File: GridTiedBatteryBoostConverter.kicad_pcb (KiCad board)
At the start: 2 copper layers, 270.1 x 143.1 mm, 161 parts, among them J101 Battery Connection, J103 Solar Panels, J202 Conn_01x03_Female, J203 I2C_BUS, J401 Screw_Terminal_01x02, J402 AudioJack2_SwitchT, Q101 IXFP36N20X3, Q102 BC847B-13-F, Q103 SSM3K329R, Q104 SSM3J334R, Q201 SSM3K329R, Q202 SSM3K329R, Q203 SSM3J334R, Q301 BC847B-13-F, Q302 BC856B-13-F, Q305 TK32A12N1,S4X, Q306 TK32A12N1,S4X, SW201 SW_Up, SW202 SW_Down, SW203 SW_Enter, U101 OPA2837IDGKR, U102 UCC2800DTR, U201 LCD 2004A Right Angle Header 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, U202 Teensy-LC, U203 PCF8574ADWR, U204 ESP-WROOM-02U, U301 FDA217, U302 LTC7138EMSE-PBF, U303 TPS560200DBVR, U304 TLV70430DBVT, U305 REF2925AIDBZT, U306 TPS560200DBVR

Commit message: change how the current sense traces attach to the average output current sense resistor R120, they are now at right angles to the current sense resistor and attach directly to it.
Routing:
- net Net-(J103-Pad2): track 102.8 -> 135.4 mm, vias 2 -> 3
- net 0: track 311.2 -> 342.9 mm, vias 87 -> 88
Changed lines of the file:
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@@
     (thickness 1.6)
     (drawings 38)
-    (tracks 1093)
+    (tracks 1105)
     (zones 0)
     (modules 161)
@@
   )
   (setup
-    (last_trace_width 5)
+    (last_trace_width 1)
     (user_trace_width 0.5)
     (user_trace_width 1)
@@
   (segment (start 275.5 64.6) (end 256.1 64.6) (width 5) (layer F.Cu) (net 3))
   (segment (start 256.1 64.6) (end 255.95 64.45) (width 5) (layer F.Cu) (net 3))
-  (via (at 234.7 64.6) (size 0.8) (drill 0.4) (layers F.Cu B.Cu) (net 3))
-  (segment (start 255.2 64.6) (end 234.7 64.6) (width 1) (layer B.Cu) (net 3))
-  (segment (start 234.7 64.6) (end 222.1 64.6) (width 1) (layer F.Cu) (net 3))
-  (segment (start 222.1 64.6) (end 211.75 74.95) (width 1) (layer F.Cu) (net 3))
-  (segment (start 211.75 74.95) (end 211.75 78) (width 1) (layer F.Cu) (net 3))
-  (segment (start 211.75 78) (end 206.35 83.4) (width 1) (layer F.Cu) (net 3))
-  (segment (start 206.35 83.4) (end 201.75 83.4) (width 1) (layer F.Cu) (net 3))
   (segment (start 194.4 115.65) (end 196.8 115.7) (width 1) (layer F.Cu) (net 3))
   (via (at 196.8 115.7) (size 0.8) (drill 0.4) (layers F.Cu B.Cu) (net 3))
@@
   (segment (start 185.3 71.90002) (end 180.1 66.70002) (width 1) (layer F.Cu) (net 3))
   (segment (start 185.3 78.05) (end 185.3 71.90002) (width 1) (layer F.Cu) (net 3))
+  (segment (start 278.4 64.6) (end 278.4 61.6) (width 1) (layer F.Cu) (net 3))
+  (via (at 251.7 60.45) (size 0.8) (drill 0.4) (layers F.Cu B.Cu) (net 3))
+  (segment (start 278.4 61.6) (end 277.25 60.45) (width 1) (layer F.Cu) (net 3))
+  (segment (start 277.25 60.45) (end 251.7 60.45) (width 1) (layer F.Cu) (net 3))
+  (via (at 234.65 61.6) (size 0.8) (drill 0.4) (layers F.Cu B.Cu) (net 3))
+  (segment (start 251.7 60.45) (end 235.8 60.45) (width 1) (layer B.Cu) (net 3))
+  (segment (start 235.8 60.45) (end 234.65 61.6) (width 1) (layer B.Cu) (net 3))
+  (segment (start 206.35 83.4) (end 201.75 83.4) (width 1) (layer F.Cu) (net 3))
+  (segment (start 211.75 78) (end 206.35 83.4) (width 1) (layer F.Cu) (net 3))
+  (segment (start 234.65 61.6) (end 219.5 61.6) (width 1) (layer F.Cu) (net 3))
+  (segment (start 211.75 69.35) (end 211.75 78) (width 1) (layer F.Cu) (net 3))
+  (segment (start 219.5 61.6) (end 211.75 69.35) (width 1) (layer F.Cu) (net 3))
   (segment (start 231.1 32) (end 216.9 32) (width 12) (layer F.Cu) (net 4))
   (segment (start 231.1 32) (end 242.9 32) (width 12) (layer F.Cu) (net 4))
@@
   (segment (start 258.6 84.85) (end 259.15 85.4) (width 1) (layer B.Cu) (net 125))
   (segment (start 203.4 84.85) (end 200.95 87.3) (width 1) (layer F.Cu) (net 125))
-  (via (at 224.85 84.9) (size 0.8) (drill 0.4) (layers F.Cu B.Cu) (net 125))
-  (segment (start 224.85 84.9) (end 258.6 84.85) (width 1) (layer B.Cu) (net 125))
   (segment (start 200.95 87.3) (end 196.55 87.3) (width 1) (layer F.Cu) (net 125))
-  (segment (start 224.85 84.9) (end 203.4 84.85) (width 1) (layer F.Cu) (net 125))
+  (via (at 249.1 70.35) (size 0.8) (drill 0.4) (layers F.Cu B.Cu) (net 125))
+  (segment (start 279.1 70.35) (end 249.1 70.35) (width 1) (layer F.Cu) (net 125))
+  (via (at 235.5 69) (size 0.8) (drill 0.4) (layers F.Cu B.Cu) (net 125))
+  (segment (start 249.1 70.35) (end 247.75 69) (width 1) (layer B.Cu) (net 125))
+  (segment (start 247.75 69) (end 235.5 69) (width 1) (layer B.Cu) (net 125))
+  (segment (start 235.5 69) (end 214.5 69) (width 1) (layer F.Cu) (net 125))
+  (segment (start 214.5 69) (end 213.65 69.85) (width 1) (layer F.Cu) (net 125))
+  (segment (start 213.65 78.4) (end 207.191163 84.858837) (width 1) (layer F.Cu) (net 125))
+  (segment (start 213.65 69.85) (end 213.65 78.4) (width 1) (layer F.Cu) (net 125))
+  (segment (start 207.191163 84.858837) (end 203.4 84.85) (width 1) (layer F.Cu) (net 125))
   (zone (net 0) (net_name "") (layer B.Cu) (hatch edge 0.508)
     (connect_pads (clearance 0.508))

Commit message: further improved routing of sense trace to current sense resistor R120
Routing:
- net 0: track 342.9 -> 338.7 mm
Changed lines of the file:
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@@
   (segment (start 185.3 71.90002) (end 180.1 66.70002) (width 1) (layer F.Cu) (net 3))
   (segment (start 185.3 78.05) (end 185.3 71.90002) (width 1) (layer F.Cu) (net 3))
-  (segment (start 278.4 64.6) (end 278.4 61.6) (width 1) (layer F.Cu) (net 3))
-  (via (at 251.7 60.45) (size 0.8) (drill 0.4) (layers F.Cu B.Cu) (net 3))
-  (segment (start 278.4 61.6) (end 277.25 60.45) (width 1) (layer F.Cu) (net 3))
-  (segment (start 277.25 60.45) (end 251.7 60.45) (width 1) (layer F.Cu) (net 3))
-  (via (at 234.65 61.6) (size 0.8) (drill 0.4) (layers F.Cu B.Cu) (net 3))
-  (segment (start 251.7 60.45) (end 235.8 60.45) (width 1) (layer B.Cu) (net 3))
-  (segment (start 235.8 60.45) (end 234.65 61.6) (width 1) (layer B.Cu) (net 3))
+  (segment (start 279.1 66.35) (end 277.8 66.35) (width 1) (layer F.Cu) (net 3))
+  (via (at 249.75 68.4) (size 0.8) (drill 0.4) (layers F.Cu B.Cu) (net 3))
+  (segment (start 277.8 66.35) (end 275.75 68.4) (width 1) (layer F.Cu) (net 3))
+  (segment (start 275.75 68.4) (end 249.75 68.4) (width 1) (layer F.Cu) (net 3))
+  (segment (start 249.75 68.4) (end 248.4 67.05) (width 1) (layer B.Cu) (net 3))
+  (via (at 235.65 67.05) (size 0.8) (drill 0.4) (layers F.Cu B.Cu) (net 3))
+  (segment (start 248.4 67.05) (end 235.65 67.05) (width 1) (layer B.Cu) (net 3))
+  (segment (start 235.65 67.05) (end 214.4 67.05) (width 1) (layer F.Cu) (net 3))
   (segment (start 206.35 83.4) (end 201.75 83.4) (width 1) (layer F.Cu) (net 3))
   (segment (start 211.75 78) (end 206.35 83.4) (width 1) (layer F.Cu) (net 3))
-  (segment (start 234.65 61.6) (end 219.5 61.6) (width 1) (layer F.Cu) (net 3))
+  (segment (start 214.4 67.05) (end 211.75 69.35) (width 1) (layer F.Cu) (net 3))
   (segment (start 211.75 69.35) (end 211.75 78) (width 1) (layer F.Cu) (net 3))
-  (segment (start 219.5 61.6) (end 211.75 69.35) (width 1) (layer F.Cu) (net 3))
   (segment (start 231.1 32) (end 216.9 32) (width 12) (layer F.Cu) (net 4))
   (segment (start 231.1 32) (end 242.9 32) (width 12) (layer F.Cu) (net 4))

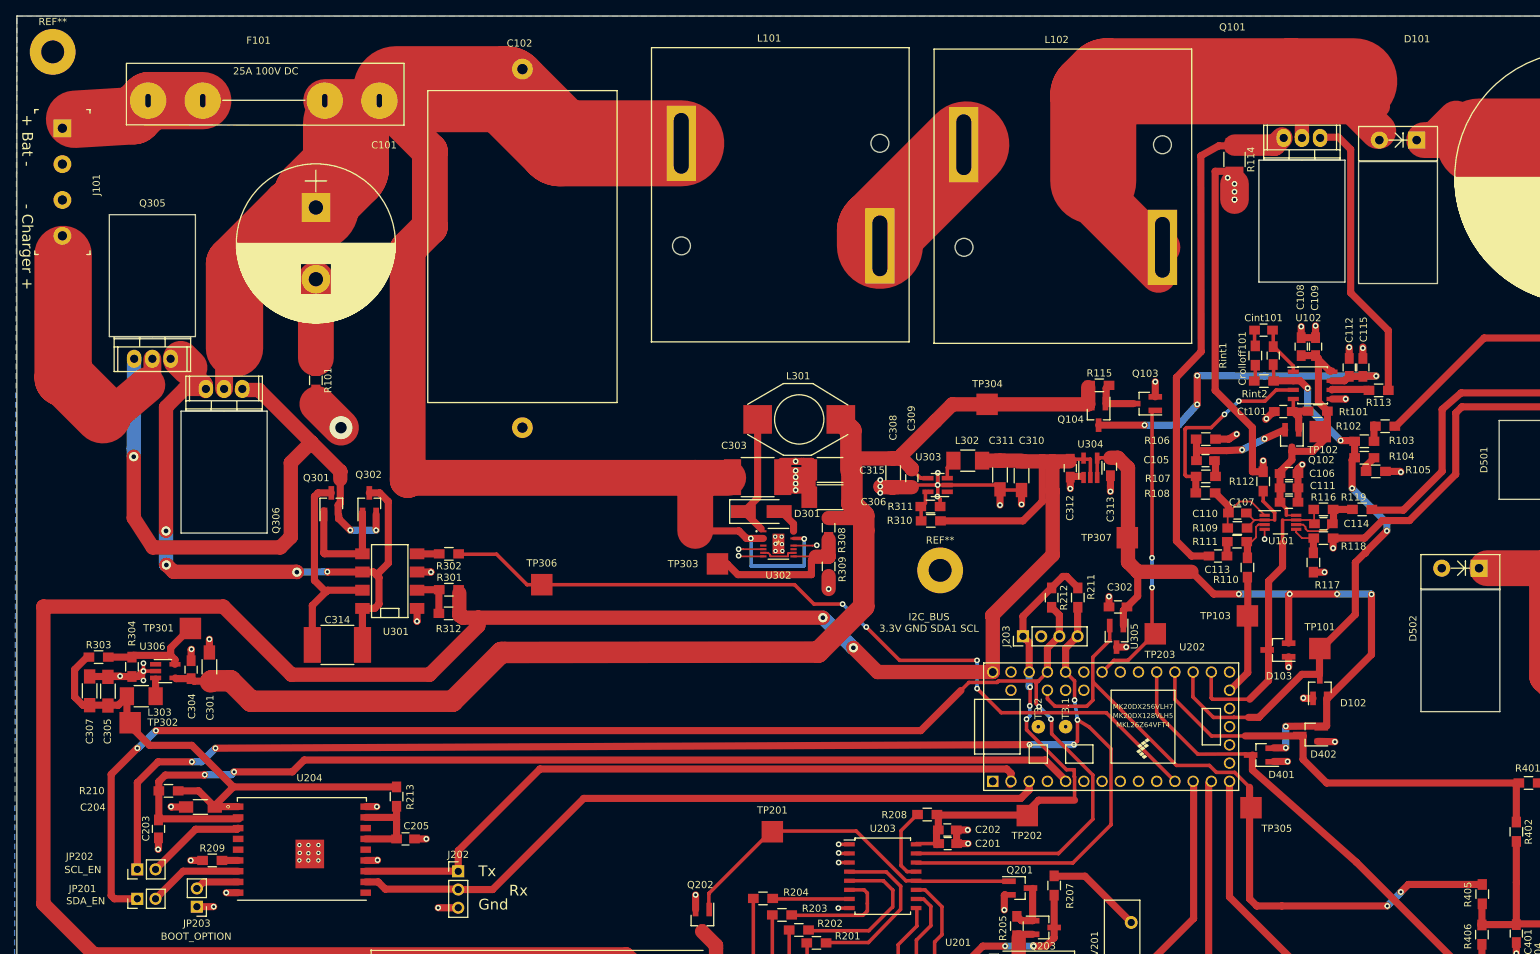
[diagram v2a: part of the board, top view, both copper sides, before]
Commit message: Replaced TK32A12N1,S4X TO-220 Toshiba transistors that were use for turning the charger on and off, with a pair of IRFP4321PBF's from Infinion, in a TO-247AC package.  The reson for the change was this part of the circuit carries ~20A at 102.2V peak, so for a 30 degree rise in trace temp with 2 Once copper we need 5mm trace width, but we also need 1.1mm clearance, and this was differcult to acheive with the to-220 package, with out bending the legs etc. These devices are 2 time the price at about  with 15.5 mOhm vs 11 mOhm rds on.  Increased the main FETs gate drive trace to 2mm from 1mm.
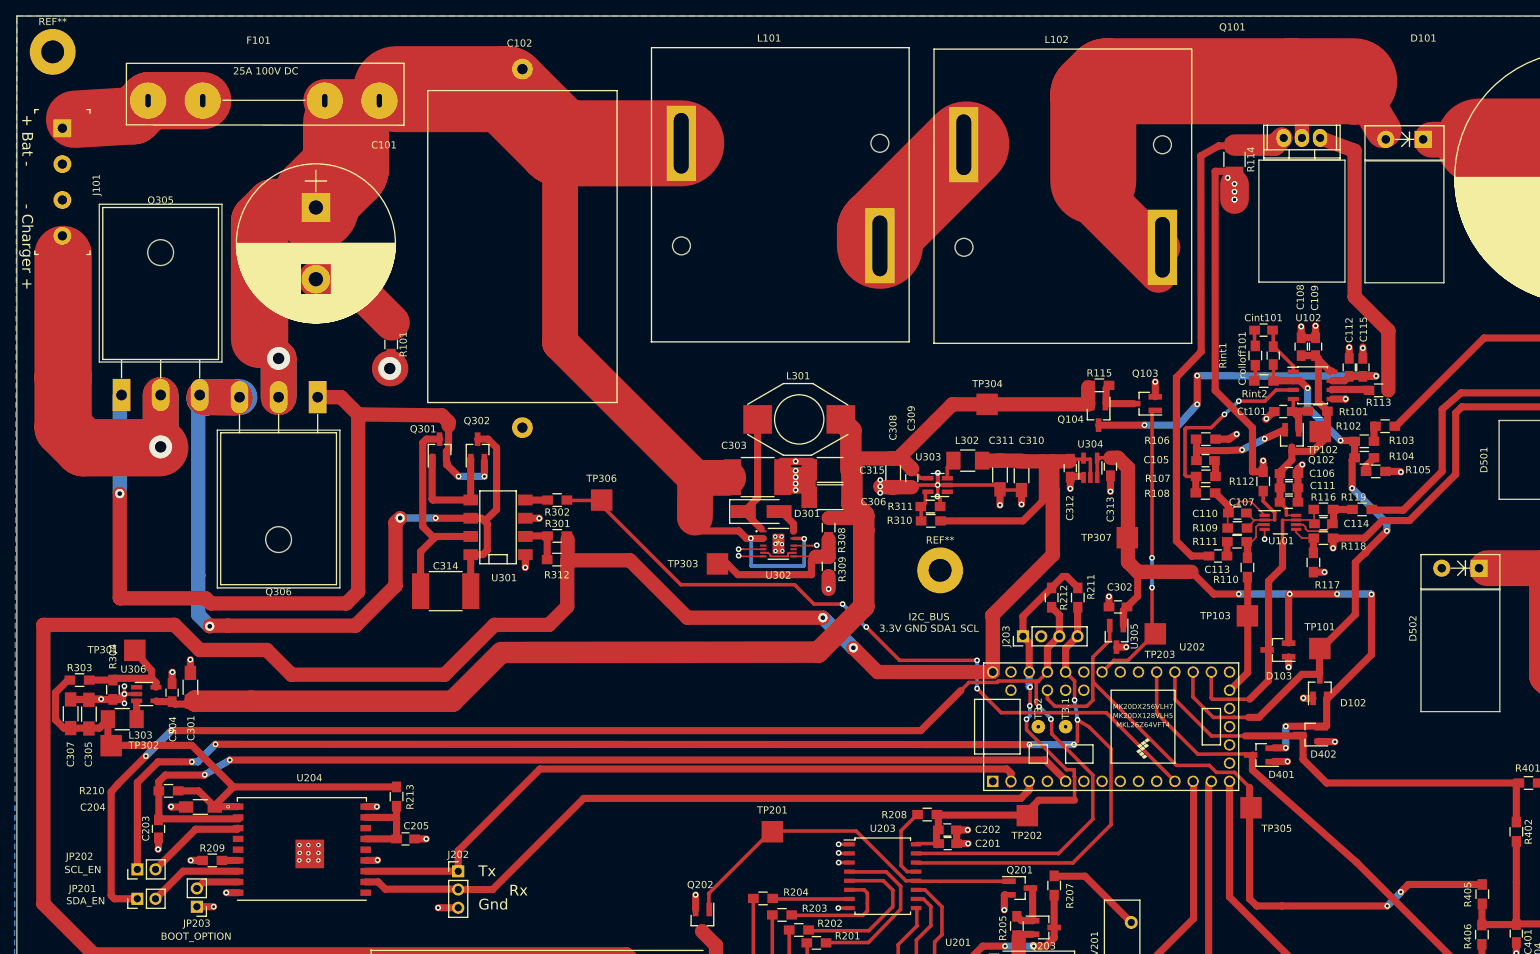
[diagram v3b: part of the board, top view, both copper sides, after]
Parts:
- Q305, Q306: value TK32A12N1,S4X -> IRFP4321PBF; footprint Transistors_ThroughHole_jl:TO-220 -> Transistors_ThroughHole_jl:TO-247-3_Horizontal_TabDown
- moved Q301 16.9 mm to (72.0, 75.0)
- moved Q302 16.9 mm to (77.2, 75.0)
- moved C314 16.9 mm to (72.8, 94.7)
- moved R301 16.9 mm to (88.3, 87.0)
- moved R302 16.9 mm to (88.3, 82.0)
- moved R312 16.9 mm to (88.3, 90.3)
- moved U301 16.9 mm to (80.1, 85.8)
- moved TP306 14.5 mm to (94.5, 82.0)
- moved Q306 13.1 mm to (55.0, 67.7)
- moved R101 11.6 mm to (65.2, 60.3)
- moved TP301 8.33 mm to (29.4, 103.0)
- moved Q305 6.63 mm to (27.6, 67.3)
- moved L303 4.15 mm to (27.7, 112.5)
- moved R304 4.15 mm to (26.4, 108.5)
- moved TP302 4.15 mm to (26.1, 116.2)
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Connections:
- net Net-(C314-Pad2) renamed /PowerSupplies/Charger_FETs_Source
- net Net-(Q101-Pad1) renamed /GateDrive
- net Net-(Q301-Pad2) renamed /PowerSupplies/Charger_Fets_GateDrive
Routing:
- net Vin: track 244.7 -> 210.5 mm, vias 2 -> 3
- net /PowerSupplies/Charger_FETs_Source: track 90.5 -> 123.9 mm, vias 4 -> 3
- net /PowerSupplies/Charger_Fets_GateDrive: track 97.3 -> 120.8 mm
- net ChargerConnection: track 36.5 -> 53.4 mm, vias 0 -> 1
- net /PowerSupplies/CHARGER_ON_OFF: track 115.4 -> 104.2 mm
- net 0: track 338.7 -> 334.1 mm
- net +5V: track 414.9 -> 418.3 mm
- net Net-(C101-Pad2): track 11.0 -> 13.1 mm
- net Net-(D101-Pad2): track 109.0 -> 107.3 mm
- net SDA1: track 216.7 -> 215.3 mm
- net Vboost_out: track 169.5 -> 170.6 mm
- net +3.3V_wifi_only: track 73.4 -> 74.3 mm
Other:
- net class ChargerConnection added: clearance 1.1, trace_width 8, via_dia 5, via_drill 2.5
- net class ChargerFetsGateDrive added: clearance 1.1, trace_width 1, via_dia 1.2, via_drill 0.6
- net class u302 removed

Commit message: Change footprint for the main switching FET to have a bent drain to achieve trace width and clearance requirements.  Fixed a pin numbering miss alignment between schematic and footprint for the isolating transformer. Spoted trace clearance issue on the 230V AC mains input into the isolating transformer for the house voltage sense, increased to 2.5mm.
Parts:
- Q101: footprint Transistors_ThroughHole_jl:TO-220 -> Transistors_ThroughHole_jl:TO-220_Horizontal_Offset_Drain
- moved R402 7.70 mm to (222.3, 120.5)
- moved R401 5.23 mm to (228.5, 119.2)
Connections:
- net Net-(J401-Pad1) renamed /MainsPowerMonitor/AC_Mains_Phase
- net Net-(J401-Pad2) renamed /MainsPowerMonitor/AC_Mains_Neutral
- TR401 pad 5: Net-(C401-Pad1) -> Net-(R401-Pad1)
- TR401 pad 6: Net-(R401-Pad1) -> Net-(C401-Pad1)
- TR401 pad 7: Net-(C401-Pad1) -> Net-(R401-Pad1)
- TR401 pad 8: Net-(R401-Pad1) -> Net-(C401-Pad1)
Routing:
- net /MainsPowerMonitor/AC_Mains_Phase: track 24.3 -> 57.8 mm
- net Vboost_out: track 170.6 -> 150.2 mm
- net Net-(R401-Pad1): track 21.0 -> 38.8 mm
- net Mains_Current: track 128.8 -> 141.1 mm
- net Net-(D101-Pad2): track 107.3 -> 101.4 mm
- net Net-(C401-Pad1): track 114.4 -> 119.4 mm
- net +5V: track 418.3 -> 420.4 mm
- net Mains_Voltage: track 63.9 -> 62.3 mm
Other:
- net class AC_Mains added: clearance 2.5, trace_width 1, via_dia 1.2, via_drill 0.6
- board text added: "Voltage Sense Phase Neutral"

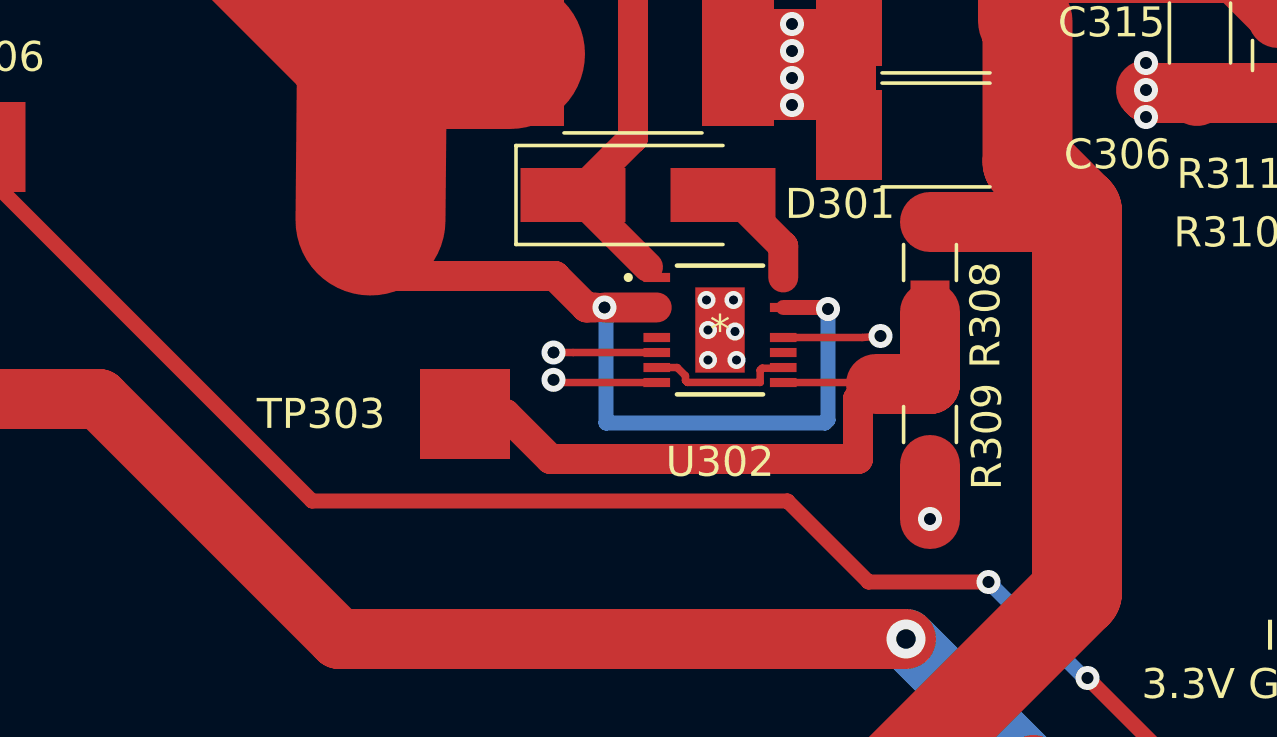
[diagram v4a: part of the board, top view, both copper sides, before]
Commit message: Improved clearance of Vin into U302 as good as the package will allow. Also reduced clearance around the Teesy to 0.5mm, because I notice one for the grounds was not connected.
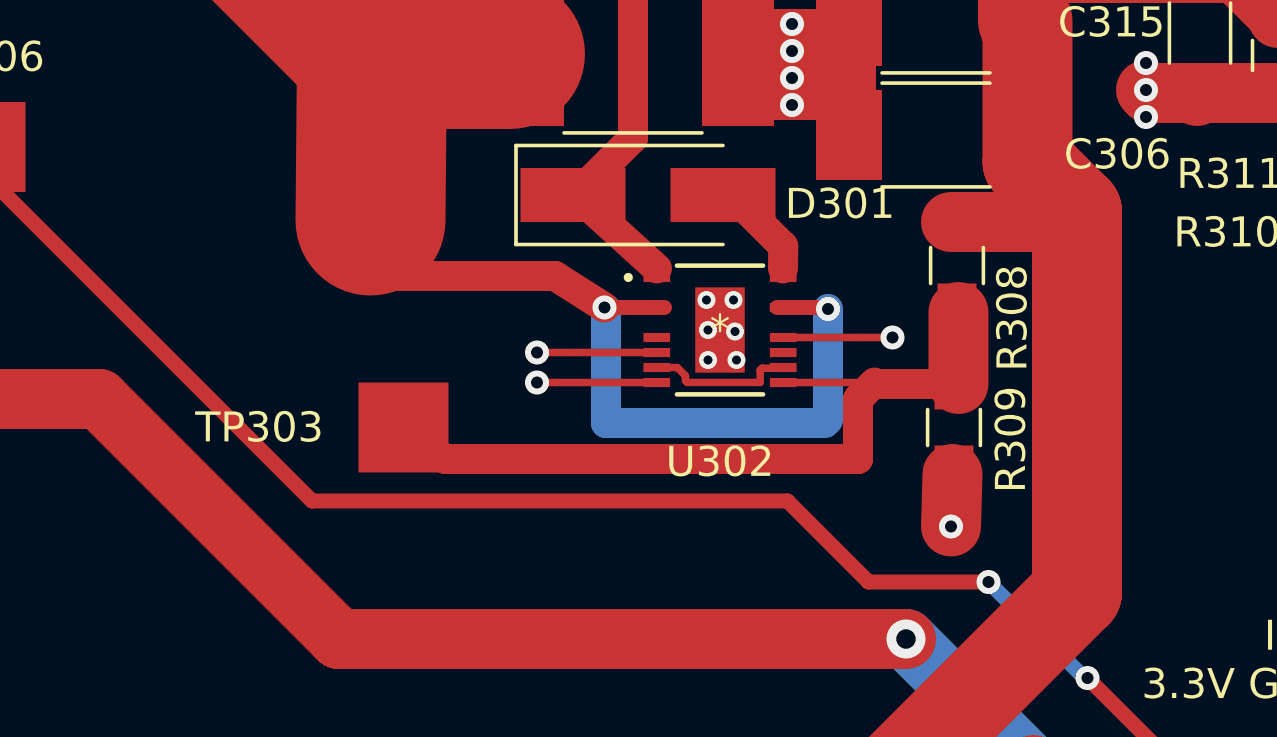
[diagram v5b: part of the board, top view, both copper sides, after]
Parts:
- moved TP303 2.10 mm to (108.7, 91.3)
- moved R308 0.91 mm to (127.1, 86.0)
- moved R309 0.81 mm to (127.0, 91.3)
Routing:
- net Net-(R308-Pad2): track 23.8 -> 26.5 mm
- net 0: track 334.1 -> 335.6 mm
- net +11V: track 179.1 -> 178.4 mm
- net Vin: track 210.5 -> 211.1 mm
